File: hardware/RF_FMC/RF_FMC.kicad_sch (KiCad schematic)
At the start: 32 parts, among them CN1 FMC_Mezzanine, Q1 SI1539CDL-T1-GE3, Q2 SI1539CDL-T1-GE3, Q3 SI1539CDL-T1-GE3, Q4 Si7141DP, Q5 Si7141DP, Q6 Si7141DP, U1 24LC024-I/SN

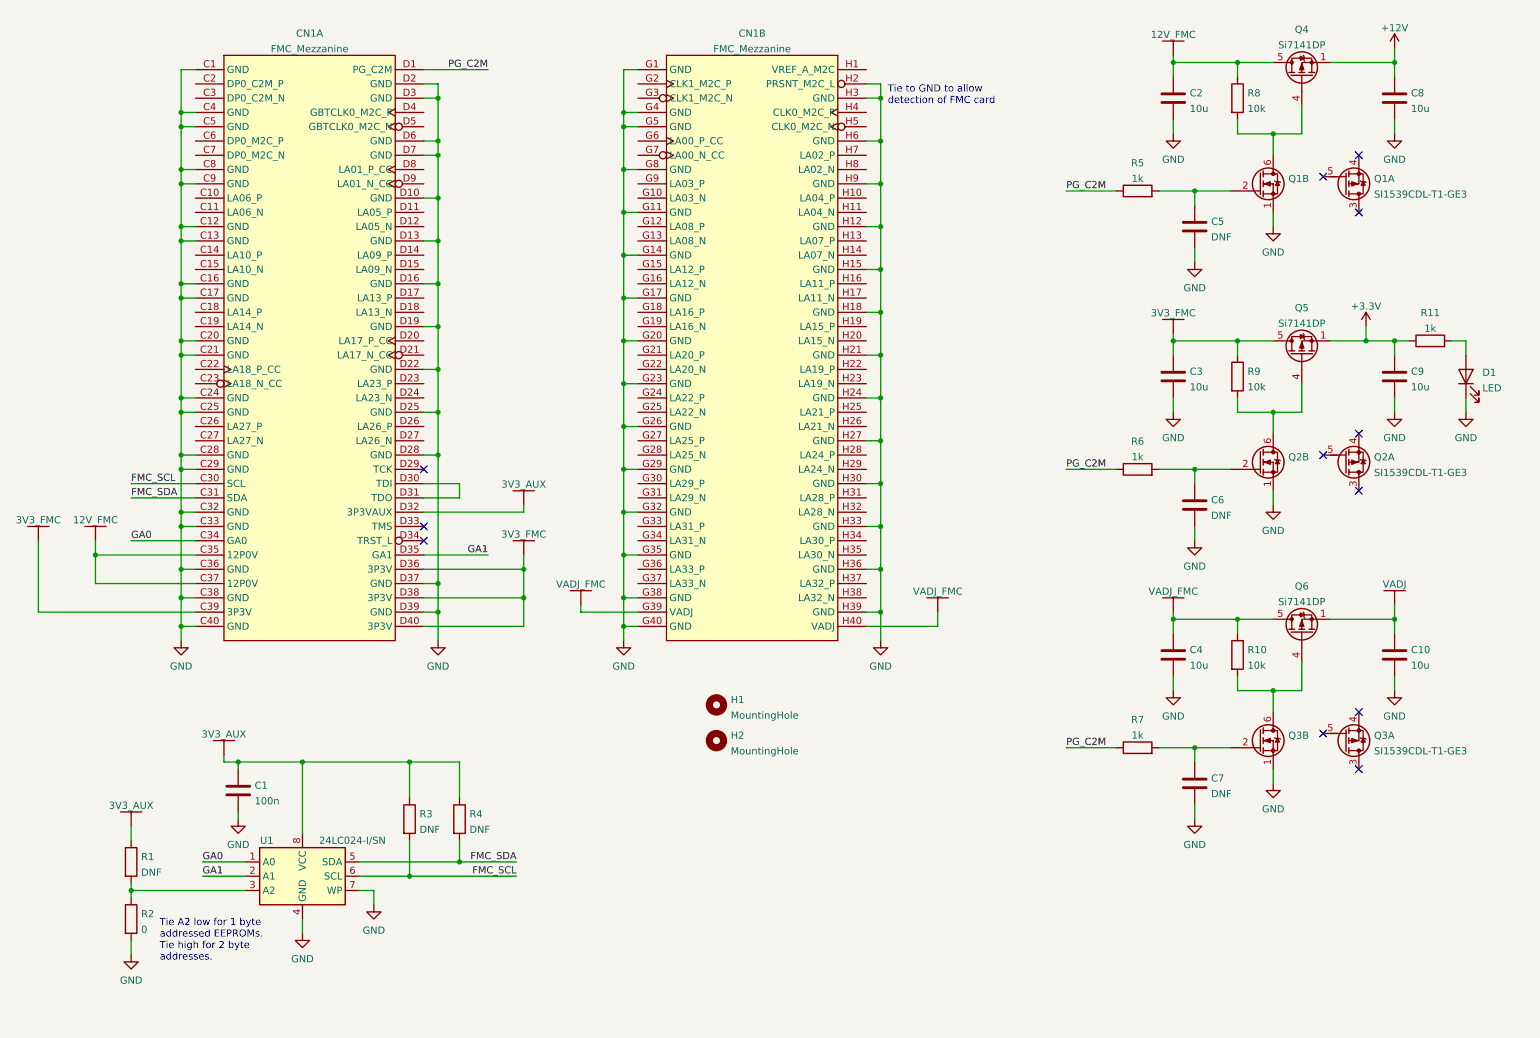
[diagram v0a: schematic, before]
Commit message: Redid FMC template to parts I can actually buy!
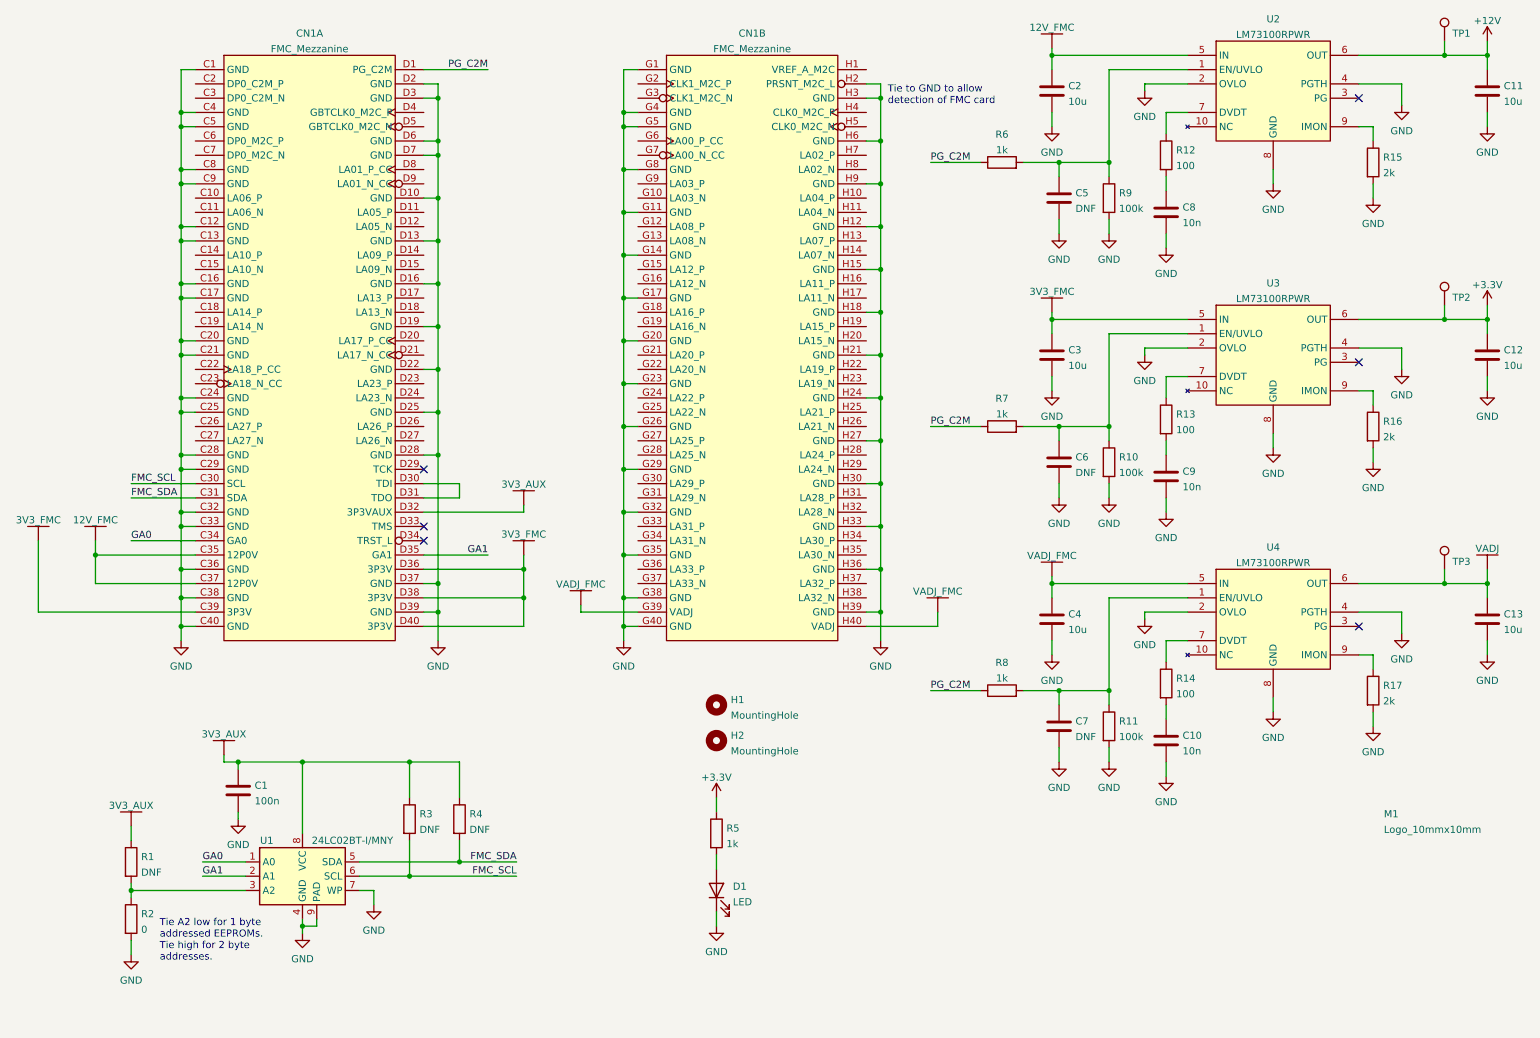
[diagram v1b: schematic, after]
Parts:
- removed Q1, Q2, Q3: SI1539CDL-T1-GE3, Package_TO_SOT_SMD:SOT-363_SC-70-6, symbol FET_WUT:SI1539CDL-T1-GE3
- removed Q4, Q5, Q6: Si7141DP, Package_SO:PowerPAK_SO-8_Single, symbol Transistor_FET:Si7141DP
- removed R6: 1k, Resistor_SMD:R_0402_1005Metric, symbol Device:R
- added C12, C13: 10u, Capacitor_SMD:C_0805_2012Metric, symbol Device:C
- added C8: 10n, Capacitor_SMD:C_0402_1005Metric, symbol Device:C
- added M1: Logo_10mmx10mm, Misc_WUT:Logo_10mmx10mm, symbol Misc_WUT:Logo_10mmx10mm
- added R12, R13, R14: 100, Resistor_SMD:R_0402_1005Metric, symbol Device:R
- added R15, R16, R17: 2k, Resistor_SMD:R_0402_1005Metric, symbol Device:R
- added R5: 1k, Resistor_SMD:R_0402_1005Metric, symbol Device:R
- added TP1, TP2, TP3: TestPoint, TestPoint:TestPoint_THTPad_D1.5mm_Drill0.7mm, symbol Connector:TestPoint
- added U2, U3, U4: LM73100RPWR, IC_WUT:TI_LM73100_RPW, symbol IC_WUT:LM73100RPWR
- C10, C9: value 10u -> 10n; footprint Capacitor_SMD:C_0805_2012Metric -> Capacitor_SMD:C_0402_1005Metric
- R10, R9: value 10k -> 100k
- R11: value 1k -> 100k
- R8: value 10k -> 1k
- U1: value 24LC024-I/SN -> 24LC02BT-I/MNY; footprint Package_SO:SOIC-8_3.9x4.9mm_P1.27mm -> Package_DFN_QFN:DFN-8-1EP_3x2mm_P0.5mm_EP1.3x1.5mm
- renumbered C8 to C11, R5 to R6
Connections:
- net +12V: now also TP1.1, U2.6 (OUT)
- net +3V3: now also C12.1, R5.1, TP2.1, U3.6 (OUT); no longer C9.1, R11.1
- net 12V_FMC: now also U2.5 (IN); no longer R8.1
- net 3V3_FMC: now also U3.5 (IN); no longer R9.1
- net GND: now also R10.2, R11.2, R9.2, U1.9 (PAD), C12.2, C13.2, C8.2, R15.2, R16.2, R17.2, U2.2 (OVLO), U2.4 (PGTH), U2.8 (GND), U3.2 (OVLO), U3.4 (PGTH), U3.8 (GND), U4.2 (OVLO), U4.4 (PGTH), U4.8 (GND)
- net PG_C2M: now also R8.1
- net VADJ: now also C13.1, TP3.1, U4.6 (OUT); no longer C10.1
- net VADJ_FMC: now also U4.5 (IN); no longer R10.1
- net at R7.2: now also C6.1, R10.1, U3.1 (EN/UVLO); no longer C7.1
- net at C5.1, R6.2: now also R9.1, U2.1 (EN/UVLO)
- net at D1.2 (A): now also R5.2; no longer R11.2
- net at R8.2: now also C7.1, R11.1, U4.1 (EN/UVLO)
- new net: R12.1, U2.7 (DVDT)
- new net: R15.1, U2.9 (IMON)
- new net: R16.1, U3.9 (IMON)
- new net: R14.1, U4.7 (DVDT)
- new net: R17.1, U4.9 (IMON)
- new net: C9.1, R13.2
- new net: R13.1, U3.7 (DVDT)
- new net: C8.1, R12.2
- new net: C10.1, R14.2
- no-connect marks 12 -> 6
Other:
- moved on the sheet: C11, C2, C5, R6

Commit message: Now working on FMC card from template
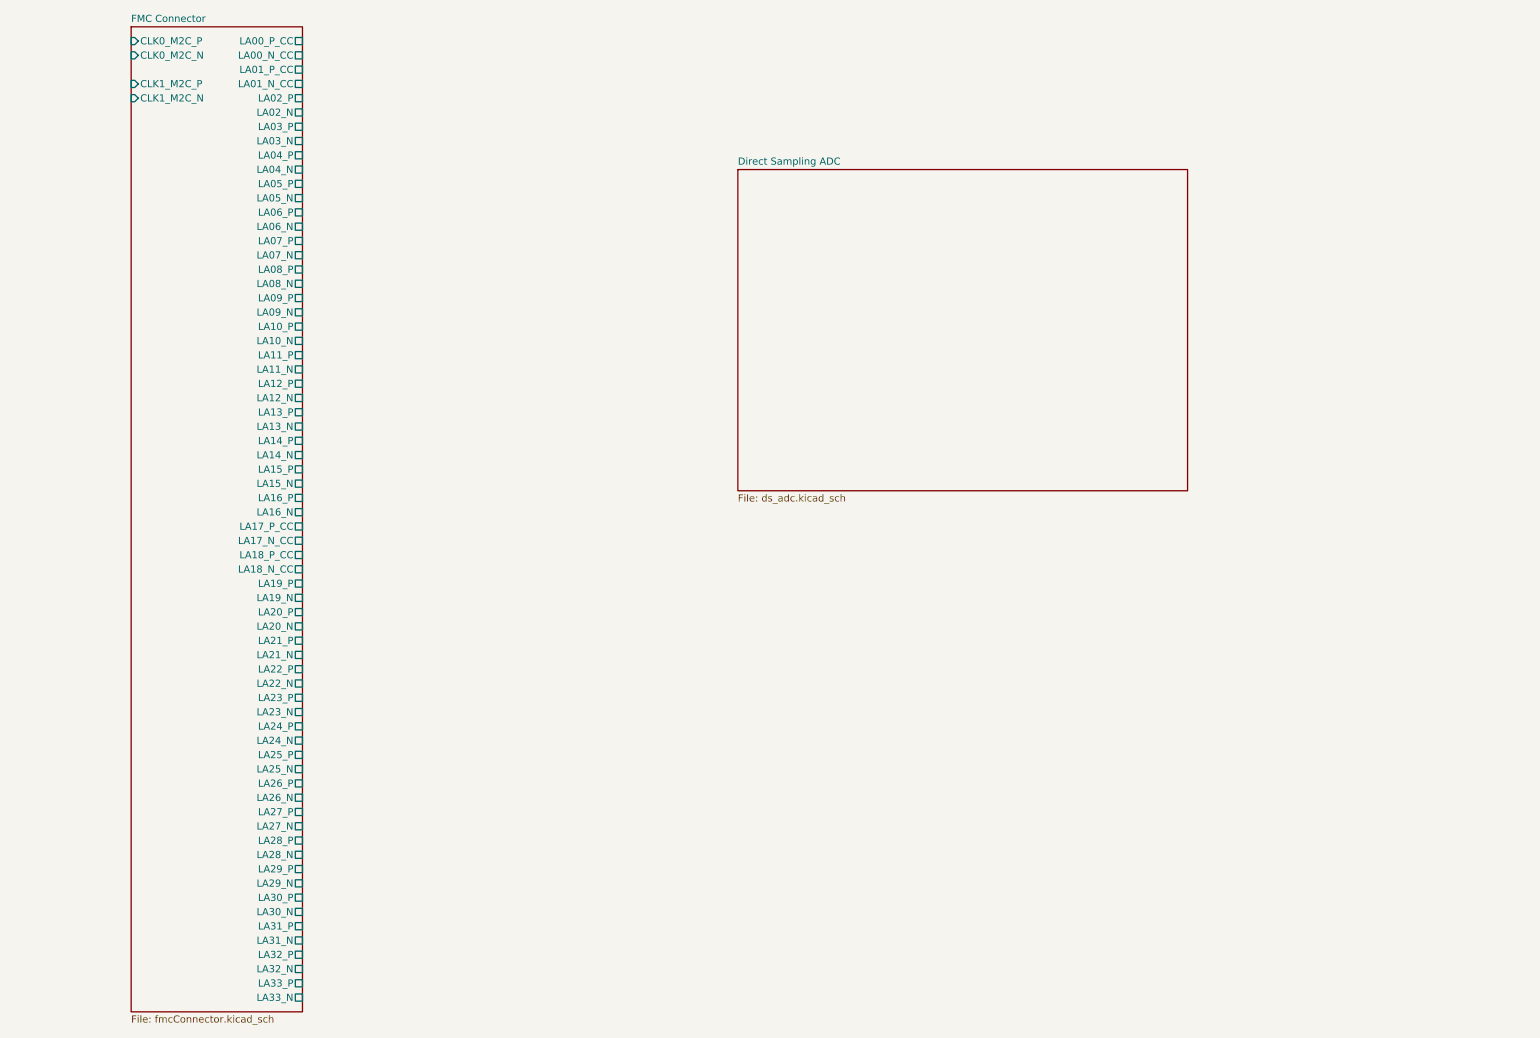
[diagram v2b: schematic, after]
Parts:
- removed C1: 100n, Capacitor_SMD:C_0402_1005Metric, symbol Device:C
- removed C10, C8, C9: 10n, Capacitor_SMD:C_0402_1005Metric, symbol Device:C
- removed C11, C12, C13, C2, C3, C4: 10u, Capacitor_SMD:C_0805_2012Metric, symbol Device:C
- removed C5, C6, C7: DNF, Capacitor_SMD:C_0402_1005Metric, symbol Device:C
- removed CN1: FMC_Mezzanine, Connector_WUT:Samtec_FMC_ASP-134604-01_4x40_Vertical, symbol Connector_WUT:FMC_Mezzanine
- removed D1: LED, LED_SMD:LED_0603_1608Metric, symbol Device:LED
- removed H1, H2: MountingHole, MountingHole:MountingHole_2.7mm, symbol Mechanical:MountingHole
- removed M1: Logo_10mmx10mm, Misc_WUT:Logo_10mmx10mm, symbol Misc_WUT:Logo_10mmx10mm
- removed R1, R3, R4: DNF, Resistor_SMD:R_0402_1005Metric, symbol Device:R
- removed R10, R11, R9: 100k, Resistor_SMD:R_0402_1005Metric, symbol Device:R
- removed R12, R13, R14: 100, Resistor_SMD:R_0402_1005Metric, symbol Device:R
- removed R15, R16, R17: 2k, Resistor_SMD:R_0402_1005Metric, symbol Device:R
- removed R2: 0, Resistor_SMD:R_0402_1005Metric, symbol Device:R
- removed R5, R6, R7, R8: 1k, Resistor_SMD:R_0402_1005Metric, symbol Device:R
- removed TP1, TP2, TP3: TestPoint, TestPoint:TestPoint_THTPad_D1.5mm_Drill0.7mm, symbol Connector:TestPoint
- removed U1: 24LC02BT-I/MNY, Package_DFN_QFN:DFN-8-1EP_3x2mm_P0.5mm_EP1.3x1.5mm, symbol Memory_EEPROM:24LC02
- removed U2, U3, U4: LM73100RPWR, IC_WUT:TI_LM73100_RPW, symbol IC_WUT:LM73100RPWR
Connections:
- no-connect marks 6 -> 0
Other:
- added sheet Direct Sampling ADC (ds_adc.kicad_sch)
- added sheet FMC Connector (fmcConnector.kicad_sch)
- note removed: "Tie A2 low for 1 byte addressed EEPROMs. Tie high for 2 byte addresses."
- note removed: "Tie to GND to allow detection of FMC card"

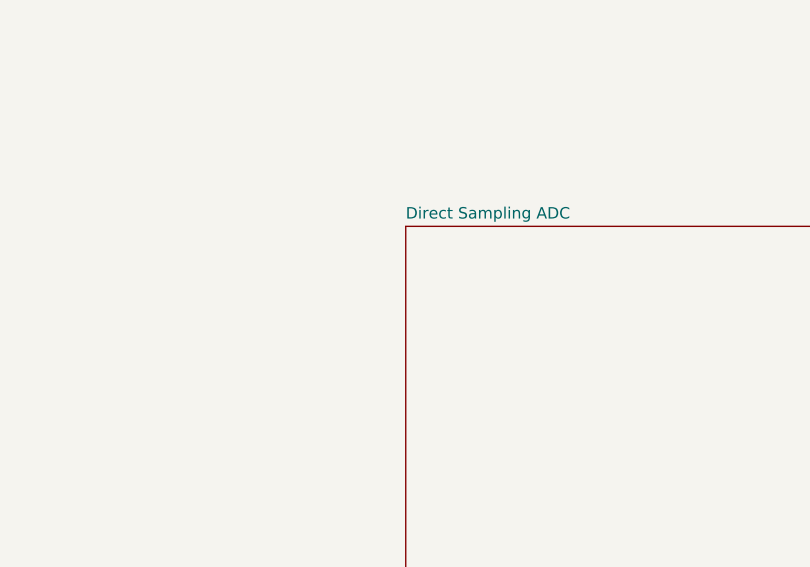
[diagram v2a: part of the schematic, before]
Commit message: Started on ADC layout
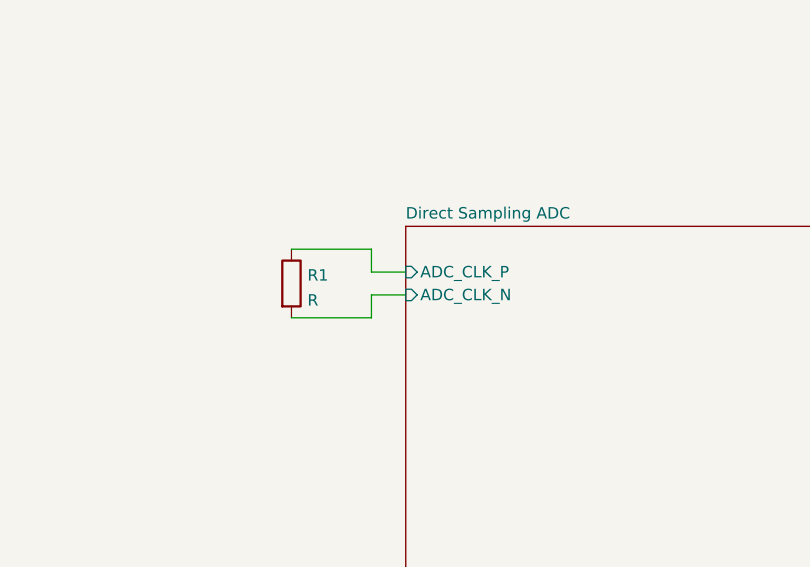
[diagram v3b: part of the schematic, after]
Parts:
- added R1: R, Resistor_SMD:R_0402_1005Metric, symbol Device:R
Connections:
- new net Direct Sampling ADC/ADC_CLK_N: R1.2
- new net Direct Sampling ADC/ADC_CLK_P: R1.1
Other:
- sheet Direct Sampling ADC ports: added ADC_CLK_N, ADC_CLK_P; removed none
